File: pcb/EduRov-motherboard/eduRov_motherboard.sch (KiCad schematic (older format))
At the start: 49 parts, among them P101 Battery connector, P102 Ext press, P103 Ext press, P104 Ext press, P105 Ch LED, Q101 IRL540NPBF, U1 Arduino header, U10 Nut, U11 Ferrules for motor cables, U12 Standoff, U13 Ferrules for motor cables, U14 Nut, U15 Ferrules for motor cables, U16 Standoff, U17 Ferrules for motor cables, U18 Nut, U19 Ferrules for motor cables, U2 Arduino header, U20 Standoff, U21 Ferrules for motor cables, U22 Nut, U23 Ferrules for motor cables, U24 Standoff, U3 Raspberry PI stacking header, U4 Temp sensor, U5 Pressure sensor, U6 Sense hat, U7 Camera, U8 JST Connector kit, U9 Ferrules for motor cables

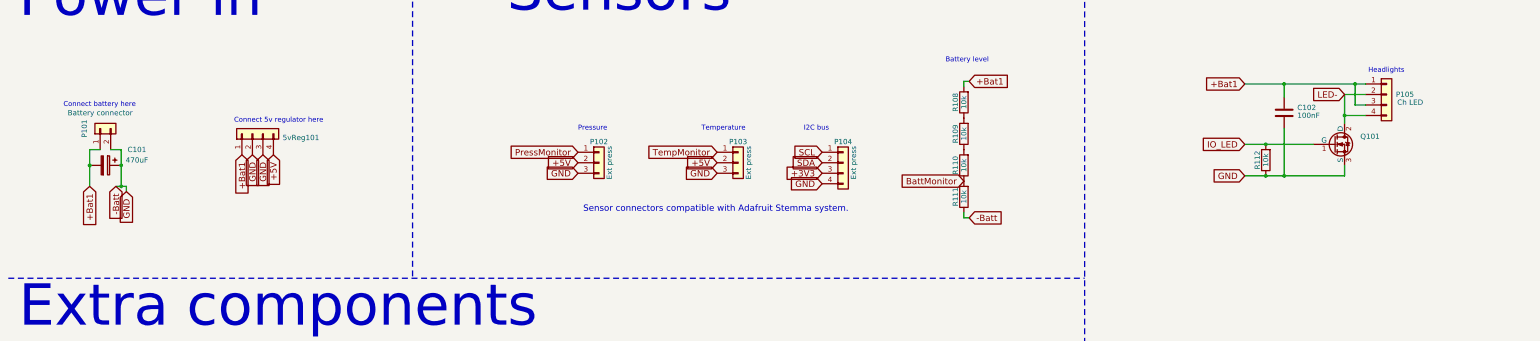
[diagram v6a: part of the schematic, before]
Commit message: Update footprints with models
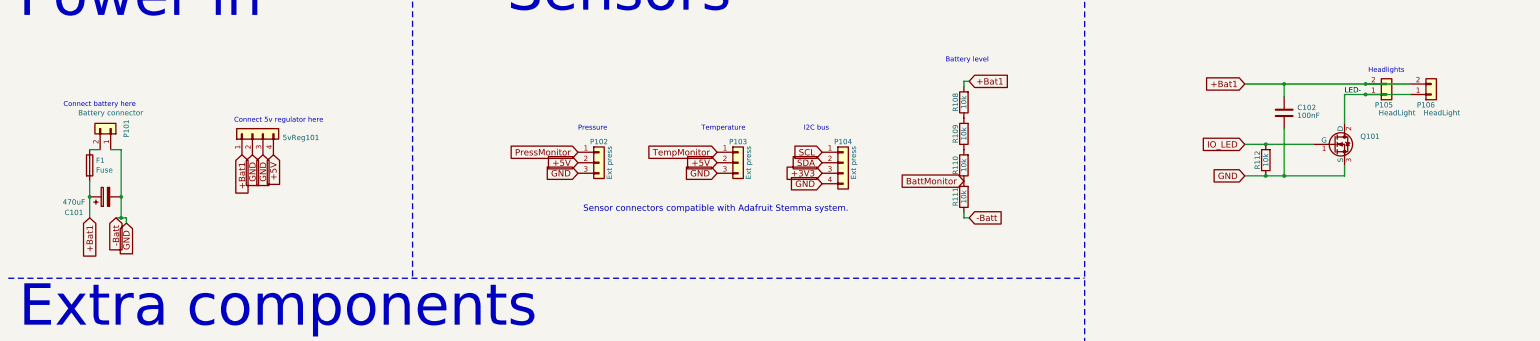
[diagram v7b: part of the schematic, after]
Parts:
- removed P105: Ch LED, Connector_JST:JST_PH_B4B-PH-K_1x04_P2.00mm_Vertical, symbol Connector_Generic:Conn_01x04
- added F1: Fuse, Fuse:Fuseholder_Blade_Mini_Keystone_3568, symbol Device:Fuse
- added P105, P106: HeadLight, Connector_PinHeader_2.54mm:PinHeader_1x02_P2.54mm_Vertical, symbol Connector_Generic:Conn_01x02
- 5vReg101: footprint Connector_PinHeader_2.54mm:PinHeader_1x04_P2.54mm_Vertical -> EduRov:iFlight_Micro
- P102, P103: footprint Connector_JST:JST_PH_B3B-PH-K_1x03_P2.00mm_Vertical -> Connector_PinHeader_2.54mm:PinHeader_1x03_P2.54mm_Horizontal
- P104: footprint Connector_JST:JST_PH_B4B-PH-K_1x04_P2.00mm_Vertical -> Connector_PinHeader_2.54mm:PinHeader_1x04_P2.54mm_Horizontal
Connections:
- net +Bat1: now also C101.1, F1.2, P105.2 (Pin_2), P106.2 (Pin_2); no longer C101.2, P101.1 (Pin_1)
- net -Batt: now also C101.2, P101.1 (Pin_1); no longer C101.1, P101.2 (Pin_2)
- net LED-: now also P105.1 (Pin_1), P106.1 (Pin_1)
- new net: F1.1, P101.2 (Pin_2)
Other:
- moved on the sheet: C101
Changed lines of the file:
@@
 F 0 "P102" H 6075 7875 50  0000 C CNN
 F 1 "Ext press" V 6175 7675 50  0000 C CNN
-F 2 "Connector_JST:JST_PH_B3B-PH-K_1x03_P2.00mm_Vertical" H 6075 7675 50  0001 C CNN
+F 2 "Connector_PinHeader_2.54mm:PinHeader_1x03_P2.54mm_Horizontal" H 6075 7675 50  0001 C CNN
 F 3 "" H 6075 7675 50  0000 C CNN
 F 4 "PHR-3" H 6075 7675 50  0001 C CNN "Part number"
@@
 Text GLabel 12225 7800 0    60   Input ~ 0
 GND
-$Comp
-L Connector_Generic:Conn_01x04 P105
-U 1 1 59D3A8DC
-P 13575 7025
-F 0 "P105" H 13750 7025 50  0000 C CNN
-F 1 "Ch LED" H 13800 6950 50  0000 C CNN
-F 2 "Connector_JST:JST_PH_B4B-PH-K_1x04_P2.00mm_Vertical" H 13575 7025 50  0001 C CNN
-F 3 "" H 13575 7025 50  0000 C CNN
-F 4 "PHR-4" H 13575 7025 50  0001 C CNN "Part number"
-F 5 "2.5mm pitch 4-pin receptacle, JST PH" H 13575 7025 50  0001 C CNN "Description"
-F 6 "JST" H 13575 7025 50  0001 C CNN "Manufacturer"
-	1    13575 7025
-	1    0    0    -1
-$EndComp
 Text GLabel 12225 6925 0    60   Input ~ 0
 +Bat1
@@
 F 0 "P103" H 7400 7875 50  0000 C CNN
 F 1 "Ext press" V 7500 7675 50  0000 C CNN
-F 2 "Connector_JST:JST_PH_B3B-PH-K_1x03_P2.00mm_Vertical" H 7400 7675 50  0001 C CNN
+F 2 "Connector_PinHeader_2.54mm:PinHeader_1x03_P2.54mm_Horizontal" H 7400 7675 50  0001 C CNN
 F 3 "" H 7400 7675 50  0000 C CNN
 F 4 "PHR-3" H 7400 7675 50  0001 C CNN "Part number"
@@
 F 0 "P104" H 8400 7875 50  0000 C CNN
 F 1 "Ext press" V 8500 7675 50  0000 C CNN
-F 2 "Connector_JST:JST_PH_B4B-PH-K_1x04_P2.00mm_Vertical" H 8400 7675 50  0001 C CNN
+F 2 "Connector_PinHeader_2.54mm:PinHeader_1x04_P2.54mm_Horizontal" H 8400 7675 50  0001 C CNN
 F 3 "" H 8400 7675 50  0000 C CNN
 F 4 "PHR-4" H 8400 7675 50  0001 C CNN "Part number"
@@
 	12425 7800 12600 7800
 Wire Wire Line
-	13375 7225 13175 7225
-Wire Wire Line
-	13175 7225 13175 7300
-Wire Wire Line
 	13375 7025 13175 7025
-Wire Wire Line
-	13175 7025 13175 7225
-Connection ~ 13175 7225
-Wire Wire Line
-	13375 6925 13275 6925
-Wire Wire Line
-	13375 7125 13275 7125
-Wire Wire Line
-	13275 7125 13275 6925
-Connection ~ 13275 6925
-Wire Wire Line
-	13275 6925 12600 6925
 Wire Wire Line
 	12600 6925 12600 7050
@@
 Wire Wire Line
 	12600 7800 13175 7800
-Text GLabel 13175 7025 0    60   Input ~ 0
-LED-
 Text Notes 5925 8150 0    60   ~ 0
 Sensor connectors compatible with Adafruit Stemma system.
@@
 F 0 "5vReg101" V 2739 7112 50  0000 R CNN
 F 1 "Conn_01x04" V 2648 7112 50  0001 R CNN
-F 2 "Connector_PinHeader_2.54mm:PinHeader_1x04_P2.54mm_Vertical" H 2775 7400 50  0001 C CNN
+F 2 "EduRov:iFlight_Micro" H 2775 7400 50  0001 C CNN
 F 3 "~" H 2775 7400 50  0001 C CNN
 F 4 "Micro" V 2775 7400 50  0001 C CNN "Part number"
@@
 $EndComp
 Wire Wire Line
-	1525 7900 1575 7900
-Connection ~ 1525 7900
-Wire Wire Line
-	1225 7550 1325 7550
-Wire Wire Line
-	1575 7900 1575 7950
-Wire Wire Line
-	1475 7900 1525 7900
-Text GLabel 1575 7950 3    60   Input ~ 0
-GND
-Text GLabel 1475 7900 3    60   Input ~ 0
+	1525 8200 1575 8200
+Connection ~ 1525 8200
+Wire Wire Line
+	1575 8200 1575 8250
+Wire Wire Line
+	1475 8200 1525 8200
+Text GLabel 1575 8250 3    60   Input ~ 0
+GND
+Text GLabel 1475 8200 3    60   Input ~ 0
 -Batt
-Connection ~ 1225 7700
-Connection ~ 1525 7700
-Wire Wire Line
-	1525 7900 1525 7700
-Wire Wire Line
-	1525 7700 1525 7550
-Wire Wire Line
-	1225 7700 1225 7550
-Wire Wire Line
-	1225 7700 1225 7900
-Text GLabel 1225 7900 3    60   Input ~ 0
+Wire Wire Line
+	1225 8000 1225 8200
+Text GLabel 1225 8200 3    60   Input ~ 0
 +Bat1
 $Comp
 L Connector_Generic:Conn_01x02 P101
 U 1 1 59F0943E
-P 1325 7350
-F 0 "P101" H 1325 7500 50  0000 C CNN
-F 1 "Battery connector" V 1475 7350 50  0000 C CNN
-F 2 "TerminalBlock_Altech:Altech_AK300_1x02_P5.00mm_45-Degree" H 1325 7350 50  0001 C CNN
-F 3 "" H 1325 7350 50  0000 C CNN
-F 4 "691137710002" H 1325 7350 50  0001 C CNN "Part number"
-F 5 "732-10955-ND" H 1325 7350 50  0001 C CNN "Digikey reference"
-F 6 "2-position terminal block, 12-30 AWG, 5mm pitch" H 1325 7350 50  0001 C CNN "Description"
-F 7 "Wurth" H 1325 7350 50  0001 C CNN "Manufacturer"
-	1    1325 7350
-	0    -1   -1   0
+P 1425 7350
+F 0 "P101" H 1425 7500 50  0000 C CNN
+F 1 "Battery connector" V 1575 7350 50  0000 C CNN
+F 2 "TerminalBlock_Altech:Altech_AK300_1x02_P5.00mm_45-Degree" H 1425 7350 50  0001 C CNN
+F 3 "" H 1425 7350 50  0000 C CNN
+F 4 "691137710002" H 1425 7350 50  0001 C CNN "Part number"
+F 5 "732-10955-ND" H 1425 7350 50  0001 C CNN "Digikey reference"
+F 6 "2-position terminal block, 12-30 AWG, 5mm pitch" H 1425 7350 50  0001 C CNN "Description"
+F 7 "Wurth" H 1425 7350 50  0001 C CNN "Manufacturer"
+	1    1425 7350
+	0    1    -1   0
 $EndComp
 $Comp
 L Device:CP C101
 U 1 1 600EBD67
-P 1375 7700
+P 1375 8000
 AR Path="/600EBD67" Ref="C101"  Part="1"
 AR Path="/5FFEC45F/600EBD67" Ref="C?"  Part="1"
@@
 AR Path="/6003F027/600EBD67" Ref="C?"  Part="1"
 AR Path="/60043462/600EBD67" Ref="C?"  Part="1"
-F 0 "C101" V 1225 8000 50  0000 C CNN
-F 1 "470uF" V 1325 8000 50  0000 C CNN
-F 2 "Capacitor_THT:CP_Radial_D12.5mm_P5.00mm" H 1413 7550 50  0001 C CNN
-F 3 "~" H 1375 7700 50  0001 C CNN
-F 4 "UVR1H471MHD1TO" V 1375 7700 50  0001 C CNN "Part number"
-F 5 "493-12789-1-ND" V 1375 7700 50  0001 C CNN "Digikey reference"
-F 6 "470uF, 20%, 50V, 5mm pitch" V 1375 7700 50  0001 C CNN "Description"
-F 7 "Nichicon" H 1375 7700 50  0001 C CNN "Manufacturer"
-	1    1375 7700
-	0    1    1    0
+F 0 "C101" V 1225 8300 50  0000 C CNN
+F 1 "470uF" V 1325 8300 50  0000 C CNN
+F 2 "Capacitor_THT:CP_Radial_D12.5mm_P5.00mm" H 1413 7850 50  0001 C CNN
+F 3 "~" H 1375 8000 50  0001 C CNN
+F 4 "UVR1H471MHD1TO" V 1375 8000 50  0001 C CNN "Part number"
+F 5 "493-12789-1-ND" V 1375 8000 50  0001 C CNN "Digikey reference"
+F 6 "470uF, 20%, 50V, 5mm pitch" V 1375 8000 50  0001 C CNN "Description"
+F 7 "Nichicon" H 1375 8000 50  0001 C CNN "Manufacturer"
+	1    1375 8000
+	0    -1   -1   0
 $EndComp
 $Comp
@@
 	1    0    0    -1
 $EndComp
+$Comp
+L Device:Fuse F1
+U 1 1 60DA2F6D
+P 1225 7700
+F 0 "F1" H 1285 7746 50  0000 L CNN
+F 1 "Fuse" H 1285 7655 50  0000 L CNN
+F 2 "Fuse:Fuseholder_Blade_Mini_Keystone_3568" V 1155 7700 50  0001 C CNN
+F 3 "~" H 1225 7700 50  0001 C CNN
+F 4 "Miniature fuse holder " H 1225 7700 50  0001 C CNN "Description"
+F 5 "36-3568-ND" H 1225 7700 50  0001 C CNN "Digikey reference"
+F 6 "3568" H 1225 7700 50  0001 C CNN "MPN"
+F 7 "Keystone Electronics" H 1225 7700 50  0001 C CNN "Manufacturer"
+F 8 "3568" H 1225 7700 50  0001 C CNN "Part number"
+	1    1225 7700
+	1    0    0    -1
+$EndComp
+Wire Wire Line
+	1525 8000 1525 8200
+Wire Wire Line
+	1225 7850 1225 8000
+Connection ~ 1225 8000
+Wire Wire Line
+	1525 7550 1525 8000
+Connection ~ 1525 8000
+Wire Wire Line
+	1225 7550 1325 7550
+$Comp
+L Connector_Generic:Conn_01x02 P105
+U 1 1 60DD0F84
+P 13575 7025
+F 0 "P105" H 13550 7125 50  0000 C CNN
+F 1 "HeadLight" H 13675 7200 50  0000 C CNN
+F 2 "Connector_PinHeader_2.54mm:PinHeader_1x02_P2.54mm_Vertical" H 13575 7025 50  0001 C CNN
+F 3 "" H 13575 7025 50  0000 C CNN
+F 4 "691137710002" H 13575 7025 50  0001 C CNN "Part number"
+F 5 "732-10955-ND" H 13575 7025 50  0001 C CNN "Digikey reference"
+F 6 "2-position terminal block, 12-30 AWG, 5mm pitch" H 13575 7025 50  0001 C CNN "Description"
+F 7 "Wurth" H 13575 7025 50  0001 C CNN "Manufacturer"
+	1    13575 7025
+	1    0    0    1
+$EndComp
+$Comp
+L Connector_Generic:Conn_01x02 P106
+U 1 1 60DD216D
+P 14000 7025
+F 0 "P106" H 13950 7125 50  0000 C CNN
+F 1 "HeadLight" H 14100 7200 50  0000 C CNN
+F 2 "Connector_PinHeader_2.54mm:PinHeader_1x02_P2.54mm_Vertical" H 14000 7025 50  0001 C CNN
+F 3 "" H 14000 7025 50  0000 C CNN
+F 4 "691137710002" H 14000 7025 50  0001 C CNN "Part number"
+F 5 "732-10955-ND" H 14000 7025 50  0001 C CNN "Digikey reference"
+F 6 "2-position terminal block, 12-30 AWG, 5mm pitch" H 14000 7025 50  0001 C CNN "Description"
+F 7 "Wurth" H 14000 7025 50  0001 C CNN "Manufacturer"
+	1    14000 7025
+	1    0    0    1
+$EndComp
+Wire Wire Line
+	13375 6925 13800 6925
+Connection ~ 13375 6925
+Wire Wire Line
+	13375 7025 13800 7025
+Connection ~ 13375 7025
+Wire Wire Line
+	12600 6925 13375 6925
+Wire Wire Line
+	13175 7025 13175 7300
+Text Label 13175 7025 0    50   ~ 0
+LED-
 $EndSCHEMATC

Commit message: Update BOM
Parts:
- added U25: Micro SD Card, symbol Edurov:Generic
- P102: Description 2.5mm pitch 3-pin receptacle, JST PH -> 2.54mm pitch 3-pin header; Digikey reference (none) -> S1111EC-03-ND; Manufacturer JST -> Sullins Connector Solutions; Part number PHR-3 -> PRPC003SBAN-M71RC
- P103: Description 2.5mm pitch 3-pin receptacle, JST PH -> 2.54mm pitch 3-pin header; Digikey Reference (none) -> S1111EC-03-ND; Digikey reference (none) -> S1111EC-03-ND; Manufacturer JST -> Sullins Connector Solutions; Part number PHR-3 -> PRPC003SBAN-M71RC
- P104: Description 2.5mm pitch 4-pin receptacle, JST PH -> 2.54mm pitch 4-pin header; Digikey reference (none) -> S1111EC-04-ND; Manufacturer JST -> Sullins Connector Solutions; Part number PHR-4 -> PRPC004SBAN-M71RC
- P105, P106: Description 2-position terminal block, 12-30 AWG, 5mm pitch -> 2.54mm pitch 2-pin header; Digikey reference 732-10955-ND -> S1011EC-02-ND; Manufacturer Wurth -> Sullins Connector Solutions; Part number 691137710002 -> PRPC002SAAN-RC
- U8: value JST Connector kit -> Jumper wires; Description JST PH connectors and crimps -> Cut and use to hook up sensors and headlights; Digikey reference 1738-1305-ND -> 1528-1960-ND; Manufacturer DFRobot -> Adafruit Industries LLC; Part number FIT0299 -> 1949
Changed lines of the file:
@@
 F 2 "Connector_PinHeader_2.54mm:PinHeader_1x03_P2.54mm_Horizontal" H 6075 7675 50  0001 C CNN
 F 3 "" H 6075 7675 50  0000 C CNN
-F 4 "PHR-3" H 6075 7675 50  0001 C CNN "Part number"
-F 5 "2.5mm pitch 3-pin receptacle, JST PH" H 6075 7675 50  0001 C CNN "Description"
-F 6 "JST" H 6075 7675 50  0001 C CNN "Manufacturer"
+F 4 "PRPC003SBAN-M71RC" H 6075 7675 50  0001 C CNN "Part number"
+F 5 "2.54mm pitch 3-pin header" H 6075 7675 50  0001 C CNN "Description"
+F 6 "Sullins Connector Solutions" H 6075 7675 50  0001 C CNN "Manufacturer"
+F 7 "S1111EC-03-ND" H 6075 7675 50  0001 C CNN "Digikey reference"
 	1    6075 7675
 	1    0    0    -1
@@
 F 2 "Connector_PinHeader_2.54mm:PinHeader_1x03_P2.54mm_Horizontal" H 7400 7675 50  0001 C CNN
 F 3 "" H 7400 7675 50  0000 C CNN
-F 4 "PHR-3" H 7400 7675 50  0001 C CNN "Part number"
-F 5 "2.5mm pitch 3-pin receptacle, JST PH" H 7400 7675 50  0001 C CNN "Description"
-F 6 "JST" H 7400 7675 50  0001 C CNN "Manufacturer"
+F 4 "PRPC003SBAN-M71RC" H 7400 7675 50  0001 C CNN "Part number"
+F 5 "2.54mm pitch 3-pin header" H 7400 7675 50  0001 C CNN "Description"
+F 6 "Sullins Connector Solutions" H 7400 7675 50  0001 C CNN "Manufacturer"
+F 7 "S1111EC-03-ND" H 7400 7675 50  0001 C CNN "Digikey Reference"
+F 8 "S1111EC-03-ND" H 7400 7675 50  0001 C CNN "Digikey reference"
 	1    7400 7675
 	1    0    0    -1
@@
 F 2 "Connector_PinHeader_2.54mm:PinHeader_1x04_P2.54mm_Horizontal" H 8400 7675 50  0001 C CNN
 F 3 "" H 8400 7675 50  0000 C CNN
-F 4 "PHR-4" H 8400 7675 50  0001 C CNN "Part number"
-F 5 "2.5mm pitch 4-pin receptacle, JST PH" H 8400 7675 50  0001 C CNN "Description"
-F 6 "JST" H 8400 7675 50  0001 C CNN "Manufacturer"
+F 4 "PRPC004SBAN-M71RC" H 8400 7675 50  0001 C CNN "Part number"
+F 5 "2.54mm pitch 4-pin header" H 8400 7675 50  0001 C CNN "Description"
+F 6 "Sullins Connector Solutions" H 8400 7675 50  0001 C CNN "Manufacturer"
+F 7 "S1111EC-04-ND" H 8400 7675 50  0001 C CNN "Digikey reference"
 	1    8400 7675
 	1    0    0    -1
@@
 P 3750 10200
 F 0 "U1" H 3928 10041 50  0001 L CNN
-F 1 "Arduino header" H 3928 9996 50  0000 L CNN
+F 1 "Arduino header" H 3928 9996 50  0001 L CNN
 F 2 "" H 3750 10200 50  0001 C CNN
 F 3 "" H 3750 10200 50  0001 C CNN
-F 4 "15 pin female through-hole header" H 3928 9905 50  0000 L CNN "Description"
+F 4 "15 pin female through-hole header" H 3928 9905 50  0001 L CNN "Description"
 F 5 "SSW-115-01-T-S" H 3750 10200 50  0001 C CNN "Part number"
 F 6 "SAM1213-15-ND" H 3750 10200 50  0001 C CNN "Digikey reference"
@@
 L Edurov:Generic U2
 U 1 1 60CA1AFC
-P 3750 10600
-F 0 "U2" H 3928 10441 50  0001 L CNN
-F 1 "Arduino header" H 3928 10396 50  0000 L CNN
-F 2 "" H 3750 10600 50  0001 C CNN
-F 3 "" H 3750 10600 50  0001 C CNN
-F 4 "15 pin female through-hole header" H 3928 10305 50  0000 L CNN "Description"
-F 5 "SSW-115-01-T-S" H 3750 10600 50  0001 C CNN "Part number"
-F 6 "SAM1213-15-ND" H 3750 10600 50  0001 C CNN "Digikey reference"
-F 7 "Samtec Inc." H 3750 10600 50  0001 C CNN "Manufacturer"
-	1    3750 10600
+P 3775 10225
+F 0 "U2" H 3953 10066 50  0001 L CNN
+F 1 "Arduino header" H 3953 10021 50  0000 L CNN
+F 2 "" H 3775 10225 50  0001 C CNN
+F 3 "" H 3775 10225 50  0001 C CNN
+F 4 "15 pin female through-hole header" H 3953 9930 50  0000 L CNN "Description"
+F 5 "SSW-115-01-T-S" H 3775 10225 50  0001 C CNN "Part number"
+F 6 "SAM1213-15-ND" H 3775 10225 50  0001 C CNN "Digikey reference"
+F 7 "Samtec Inc." H 3775 10225 50  0001 C CNN "Manufacturer"
+	1    3775 10225
 	1    0    0    -1
 $EndComp
@@
 P 3750 9800
 F 0 "U8" H 3928 9641 50  0001 L CNN
-F 1 "JST Connector kit" H 3928 9596 50  0000 L CNN
+F 1 "Jumper wires" H 3928 9596 50  0000 L CNN
 F 2 "" H 3750 9800 50  0001 C CNN
 F 3 "" H 3750 9800 50  0001 C CNN
-F 4 "JST PH connectors and crimps" H 3928 9505 50  0000 L CNN "Description"
-F 5 "FIT0299" H 3750 9800 50  0001 C CNN "Part number"
-F 6 "1738-1305-ND" H 3750 9800 50  0001 C CNN "Digikey reference"
-F 7 "DFRobot" H 3750 9800 50  0001 C CNN "Manufacturer"
+F 4 "Cut and use to hook up sensors and headlights" H 3928 9505 50  0000 L CNN "Description"
+F 5 "1949" H 3750 9800 50  0001 C CNN "Part number"
+F 6 "1528-1960-ND" H 3750 9800 50  0001 C CNN "Digikey reference"
+F 7 "Adafruit Industries LLC" H 3750 9800 50  0001 C CNN "Manufacturer"
 	1    3750 9800
 	1    0    0    -1
@@
 F 2 "Connector_PinHeader_2.54mm:PinHeader_1x02_P2.54mm_Vertical" H 13575 7025 50  0001 C CNN
 F 3 "" H 13575 7025 50  0000 C CNN
-F 4 "691137710002" H 13575 7025 50  0001 C CNN "Part number"
-F 5 "732-10955-ND" H 13575 7025 50  0001 C CNN "Digikey reference"
-F 6 "2-position terminal block, 12-30 AWG, 5mm pitch" H 13575 7025 50  0001 C CNN "Description"
-F 7 "Wurth" H 13575 7025 50  0001 C CNN "Manufacturer"
+F 4 "PRPC002SAAN-RC" H 13575 7025 50  0001 C CNN "Part number"
+F 5 "S1011EC-02-ND" H 13575 7025 50  0001 C CNN "Digikey reference"
+F 6 "2.54mm pitch 2-pin header" H 13575 7025 50  0001 C CNN "Description"
+F 7 "Sullins Connector Solutions" H 13575 7025 50  0001 C CNN "Manufacturer"
 	1    13575 7025
 	1    0    0    1
@@
 F 2 "Connector_PinHeader_2.54mm:PinHeader_1x02_P2.54mm_Vertical" H 14000 7025 50  0001 C CNN
 F 3 "" H 14000 7025 50  0000 C CNN
-F 4 "691137710002" H 14000 7025 50  0001 C CNN "Part number"
-F 5 "732-10955-ND" H 14000 7025 50  0001 C CNN "Digikey reference"
-F 6 "2-position terminal block, 12-30 AWG, 5mm pitch" H 14000 7025 50  0001 C CNN "Description"
-F 7 "Wurth" H 14000 7025 50  0001 C CNN "Manufacturer"
+F 4 "PRPC002SAAN-RC" H 14000 7025 50  0001 C CNN "Part number"
+F 5 "S1011EC-02-ND" H 14000 7025 50  0001 C CNN "Digikey reference"
+F 6 "2.54mm pitch 2-pin header" H 14000 7025 50  0001 C CNN "Description"
+F 7 "Sullins Connector Solutions" H 14000 7025 50  0001 C CNN "Manufacturer"
 	1    14000 7025
 	1    0    0    1
@@
 Text Label 13175 7025 0    50   ~ 0
 LED-
+$Comp
+L Edurov:Generic U25
+U 1 1 60E0ECB6
+P 3750 10600
+F 0 "U25" H 3928 10441 50  0001 L CNN
+F 1 "Micro SD Card" H 3928 10396 50  0000 L CNN
+F 2 "" H 3750 10600 50  0001 C CNN
+F 3 "" H 3750 10600 50  0001 C CNN
+F 4 "16GB micro SD card with NOOBS installed" H 3928 10305 50  0000 L CNN "Description"
+F 5 "SC0252F" H 3750 10600 50  0001 C CNN "Part number"
+F 6 "2648-SC0252F-ND" H 3750 10600 50  0001 C CNN "Digikey reference"
+F 7 "Raspberry Pi" H 3750 10600 50  0001 C CNN "Manufacturer"
+	1    3750 10600
+	1    0    0    -1
+$EndComp
 $EndSCHEMATC
